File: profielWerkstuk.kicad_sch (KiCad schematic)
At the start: 0 parts

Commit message: added preselectors and antenna protection
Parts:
- added AE1: HF_ANT, symbol Device:Antenna
- added AE2: VHF_ANT, symbol Device:Antenna
- added C1, C3: 1.6n, symbol Device:C
- added C10, C12, C15: 200p, symbol Device:C
- added C11: 91p, symbol Device:C
- added C13, C17: 110p, symbol Device:C
- added C14, C16: 36p, symbol Device:C
- added C18, C22: 82p, symbol Device:C
- added C19, C21: 15p, symbol Device:C
- added C2: 680p, symbol Device:C
- added C20: 130p, symbol Device:C
- added C23, C27: 62p, symbol Device:C
- added C24, C26: 7.5p, symbol Device:C
- added C25: 100p, symbol Device:C
- added C4, C6: 820p, symbol Device:C
- added C5: 360p, symbol Device:C
- added C7, C9: 430p, symbol Device:C
- added C8: 180p, symbol Device:C
- added D1, D2: D, symbol Device:D
- added L1, L3: 2u, symbol Device:L
- added L10, L12, L19, L21: 240n, symbol Device:L
- added L11: 560, symbol Device:L
- added L13, L17: 110n, symbol Device:L
- added L14, L16: 330n, symbol Device:L
- added L15: 62n, symbol Device:L
- added L18, L22: 47n, symbol Device:L
- added L2: 4.7u, symbol Device:L
- added L20: 27n, symbol Device:L
- added L23, L27: 22n, symbol Device:L
- added L24, L26: 180n, symbol Device:L
- added L25: 13n, symbol Device:L
- added L4, L6: 1u, symbol Device:L
- added L5: 2.2u, symbol Device:L
- added L7, L9: 470n, symbol Device:L
- added L8: 1.1u, symbol Device:L
- added R1, R2: 1M, symbol Device:R
- added R3, R4, R5, R6, R7, R8, R9: 50, symbol Device:R
- added SW1: SW_HF/VHFa, symbol Switch:SW_SPDT
- added SW2: SW_ANT, symbol Switch:SW_SPDT
- added SW3: SW_PRESELECT_HFa, symbol Switch:SW_Rotary_1x4_MP
- added SW4, SW6: SW_Rotary_1x3_MP, symbol Switch:SW_Rotary_1x3_MP
- added SW5: SW_PRESELECT_HFb, symbol Switch:SW_Rotary_1x4_MP
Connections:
- new net: C22.1, L21.2, L22.1, SW6.2
- new net: R7.1, SW4.1
- new net: C13.1, C14.1, L13.1, R7.2
- new net: C15.1, C16.1, L14.2, L15.1
- new net: AE1.1 (A), R1.1, SW2.3 (C)
- new net: R3.1, SW3.1
- new net: C1.1, C2.1, L1.1, R3.2
- new net: C26.2, L26.1
- new net: C27.1, L26.2, L27.1, SW6.3
- new net: C23.1, C24.1, L23.1, R9.2
- new net: C17.1, L16.2, L17.1, SW6.1
- new net: C25.1, C26.1, L24.2, L25.1
- new net: C9.1, L8.2, L9.1, SW5.3
- new net: C19.2, L19.1
- new net: C20.1, C21.1, L19.2, L20.1
- new net: R5.1, SW3.3
- new net: C7.1, C8.1, L7.1, R5.2
- new net: AE2.1 (A), R2.1, SW2.1 (A)
- new net: C6.1, L5.2, L6.1, SW5.2
- new net: C16.2, L16.1
- new net: C10.1, C11.1, L10.1, R6.2
- new net: C11.2, L11.1
- new net: C18.1, C19.1, L18.1, R8.2
- new net: C2.2, L2.1
- new net: C14.2, L14.1
- new net: D1.2 (A), D2.1 (K), SW1.2 (B), SW2.2 (B)
- new net: C3.1, L2.2, L3.1, SW5.1
- new net: C12.1, L11.2, L12.1, SW5.4
- new net: R4.1, SW3.2
- new net: R6.1, SW3.4
- new net: SW1.1 (A), SW3.5
- new net: C21.2, L21.1
- new net: C4.1, C5.1, L4.1, R4.2
- new net: C8.2, L8.1
- new net: C24.2, L24.1
- new net: R8.1, SW4.2
- new net: R9.1, SW4.3
- new net: SW1.3 (C), SW4.4
- new net: C5.2, L5.1
- new net GNDPWR: D1.1 (K), D2.2 (A), R1.2, R2.2
- new net GNDREF: C1.2, C10.2, C12.2, C13.2, C15.2, C17.2, C18.2, C20.2, C22.2, C23.2, C25.2, C27.2, C3.2, C4.2, C6.2, C7.2, C9.2, L1.2, L10.2, L12.2, L13.2, L15.2, L17.2, L18.2, L20.2, L22.2, L23.2, L25.2, L27.2, L3.2, L4.2, L6.2, L7.2, L9.2, SW3.MP, SW4.MP, SW5.MP, SW6.MP
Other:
- note added: "HF"
- note added: "VHF"

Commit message: renamed VHF preselector switch
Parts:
- L11: value 560 -> 560n
- SW1: value SW_HF/VHFa -> SW_HF/VHF
- SW4: value SW_Rotary_1x3_MP -> SW_PRESELECT_VHFa
- SW6: value SW_Rotary_1x3_MP -> SW_PRESELECT_VHFb
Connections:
- net at AE1.1 (A), R1.1: now also SW2.1 (A); no longer SW2.3 (C)
- net at AE2.1 (A), R2.1: now also SW2.3 (C); no longer SW2.1 (A)
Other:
- moved on the sheet: SW2
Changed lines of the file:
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@@
 	(wire
 		(pts
+			(xy 238.76 25.4) (xy 256.54 25.4)
+		)
+		(stroke
+			(width 0)
+			(type default)
+		)
+	)
+	(wire
+		(pts
 			(xy 144.78 88.9) (xy 158.75 88.9)
 		)
@@
 	(wire
 		(pts
+			(xy 173.99 91.44) (xy 199.39 91.44)
+		)
+		(stroke
+			(width 0)
+			(type default)
+		)
+	)
+	(wire
+		(pts
 			(xy 134.62 121.92) (xy 133.35 121.92)
 		)
@@
 			)
 		)
-		(property "Value" "SW_Rotary_1x3_MP"
+		(property "Value" "SW_PRESELECT_VHFa"
 			(at 38.1 83.82 0)
 			(show_name no)
@@
 			)
 		)
-		(property "Value" "560"
+		(property "Value" "560n"
 			(at 185.42 67.31 90)
 			(show_name no)
@@
 			)
 		)
-		(property "Value" "SW_HF/VHFa"
+		(property "Value" "SW_HF/VHF"
 			(at 87.63 21.59 0)
 			(show_name no)
@@
 			)
 		)
-		(property "Value" "SW_Rotary_1x3_MP"
+		(property "Value" "SW_PRESELECT_VHFb"
 			(at 166.37 83.82 0)
 			(show_name no)
@@
 	(symbol
 		(lib_id "Switch:SW_SPDT")
-		(at 46.99 27.94 180)
+		(at 46.99 27.94 0)
+		(mirror y)
 		(unit 1)
 		(body_style 1)
@@
 		(in_pos_files yes)
 		(dnp no)
-		(fields_autoplaced yes)
 		(property "Reference" "SW2"
 			(at 46.99 19.05 0)
@@
 		)
 		(property "Datasheet" ""
-			(at 46.99 20.32 0)
+			(at 46.99 35.56 0)
 			(hide yes)
 			(show_name no)

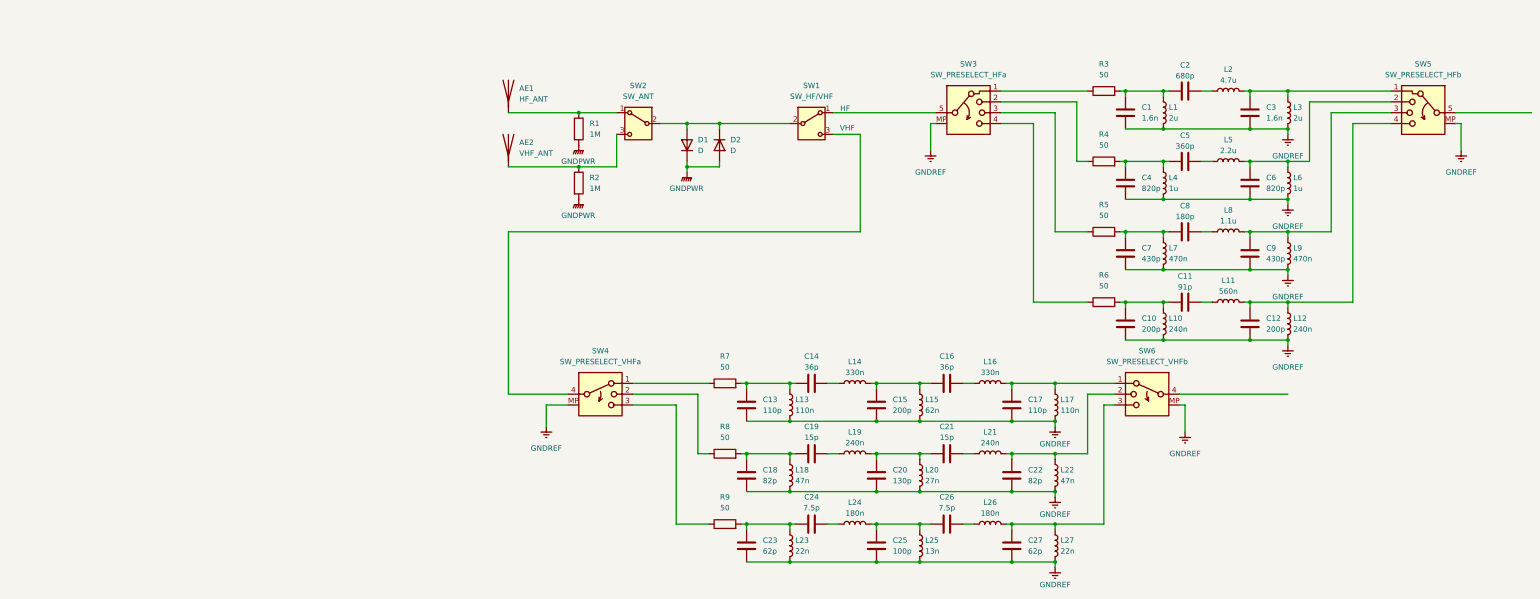
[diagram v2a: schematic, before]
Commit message: adjusted preselector values for overlap
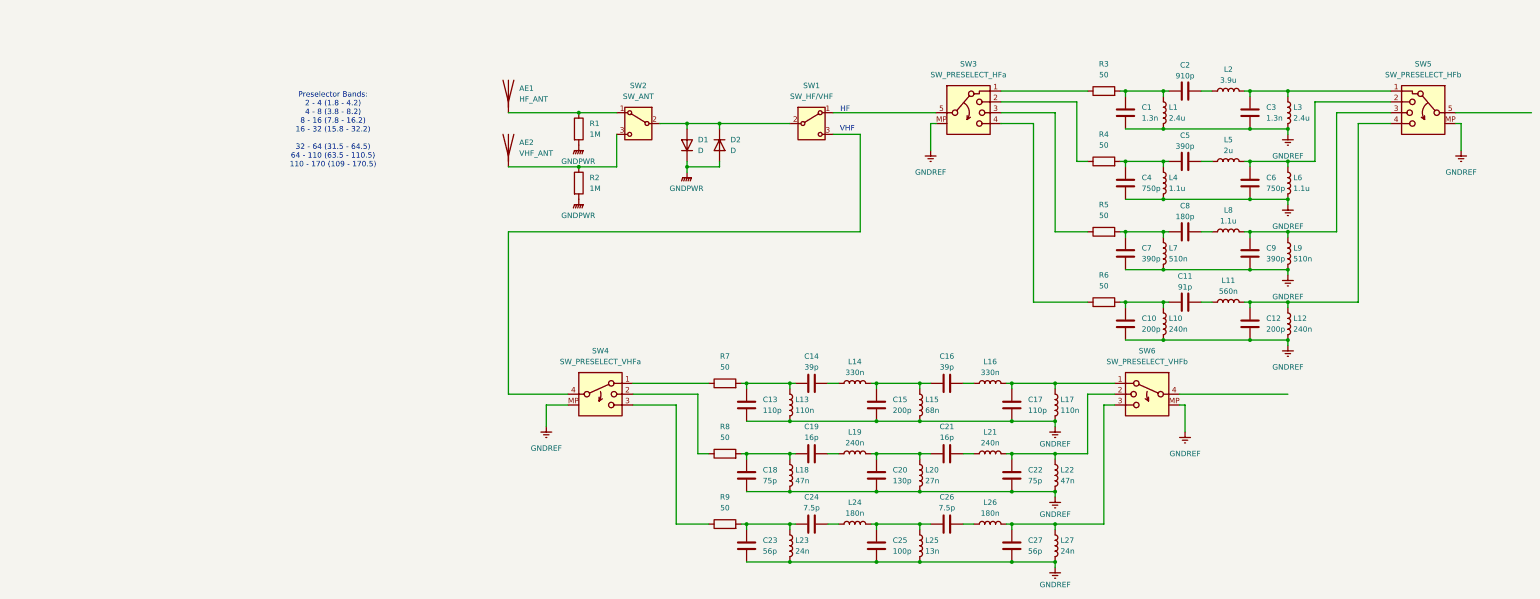
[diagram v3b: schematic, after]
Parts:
- C1, C3: value 1.6n -> 1.3n
- C14, C16: value 36p -> 39p
- C18, C22: value 82p -> 75p
- C19, C21: value 15p -> 16p
- C2: value 680p -> 910p
- C23, C27: value 62p -> 56p
- C4, C6: value 820p -> 750p
- C5: value 360p -> 390p
- C7, C9: value 430p -> 390p
- L1, L3: value 2u -> 2.4u
- L15: value 62n -> 68n
- L2: value 4.7u -> 3.9u
- L23, L27: value 22n -> 24n
- L4, L6: value 1u -> 1.1u
- L5: value 2.2u -> 2u
- L7, L9: value 470n -> 510n
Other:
- note added: "Preselector Bands: 2 - 4 (1.8 - 4.2) 4 - 8 (3.8 - 8.2) 8 - 16 (7.8 - 16.2) 16 - 32 (15.8 - 32.2) 32 - 64 (31.5 - 64.5) 64 - 110 (63.5 - 110.5) 110 - 170 (109 - 170.5)"
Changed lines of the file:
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@@
 	(generator_version "10.0")
 	(paper "A3")
+	(text "Preselector Bands:\n2 - 4 (1.8 - 4.2)\n4 - 8 (3.8 - 8.2)\n8 - 16 (7.8 - 16.2)\n16 - 32 (15.8 - 32.2)\n\n32 - 64 (31.5 - 64.5)\n64 - 110 (63.5 - 110.5)\n110 - 170 (109 - 170.5)"
+		(exclude_from_sim no)
+		(at -24.638 29.464 0)
+		(effects
+			(font
+				(size 1.27 1.27)
+			)
+		)
+	)
 	(text "HF"
 		(exclude_from_sim no)
@@
 	)
 	(junction
-		(at 199.39 36.83)
-		(diameter 0)
-		(color 0 0 0 0)
-	)
-	(junction
 		(at 102.87 105.41)
 		(diameter 0)
@@
 	)
 	(junction
+		(at 199.39 53.34)
+		(diameter 0)
+		(color 0 0 0 0)
+	)
+	(junction
 		(at 190.5 78.74)
 		(diameter 0)
@@
 	)
 	(junction
+		(at 199.39 36.83)
+		(diameter 0)
+		(color 0 0 0 0)
+	)
+	(junction
 		(at 33.02 25.4)
 		(diameter 0)
@@
 	)
 	(junction
-		(at 199.39 69.85)
-		(diameter 0)
-		(color 0 0 0 0)
-	)
-	(junction
 		(at 113.03 114.3)
 		(diameter 0)
@@
 	)
 	(junction
-		(at 82.55 105.41)
+		(at 199.39 69.85)
 		(diameter 0)
 		(color 0 0 0 0)
 	)
 	(junction
-		(at 144.78 88.9)
+		(at 82.55 105.41)
 		(diameter 0)
 		(color 0 0 0 0)
 	)
 	(junction
-		(at 199.39 53.34)
+		(at 144.78 88.9)
 		(diameter 0)
 		(color 0 0 0 0)
@@
 	(wire
 		(pts
-			(xy 204.47 22.86) (xy 223.52 22.86)
+			(xy 205.74 22.86) (xy 223.52 22.86)
 		)
 		(stroke
@@
 	(wire
 		(pts
-			(xy 204.47 36.83) (xy 204.47 22.86)
+			(xy 205.74 36.83) (xy 205.74 22.86)
 		)
 		(stroke
@@
 	(wire
 		(pts
-			(xy 214.63 69.85) (xy 199.39 69.85)
+			(xy 215.9 69.85) (xy 199.39 69.85)
 		)
 		(stroke
@@
 	(wire
 		(pts
-			(xy 199.39 36.83) (xy 204.47 36.83)
+			(xy 199.39 36.83) (xy 205.74 36.83)
 		)
 		(stroke
@@
 	(wire
 		(pts
-			(xy 223.52 27.94) (xy 214.63 27.94)
+			(xy 223.52 27.94) (xy 215.9 27.94)
 		)
 		(stroke
@@
 	(wire
 		(pts
-			(xy 209.55 25.4) (xy 209.55 53.34)
+			(xy 210.82 25.4) (xy 210.82 53.34)
 		)
 		(stroke
@@
 	(wire
 		(pts
-			(xy 209.55 53.34) (xy 199.39 53.34)
+			(xy 210.82 53.34) (xy 199.39 53.34)
 		)
 		(stroke
@@
 	(wire
 		(pts
-			(xy 214.63 27.94) (xy 214.63 69.85)
+			(xy 215.9 27.94) (xy 215.9 69.85)
 		)
 		(stroke
@@
 	(wire
 		(pts
-			(xy 223.52 25.4) (xy 209.55 25.4)
+			(xy 223.52 25.4) (xy 210.82 25.4)
 		)
 		(stroke
@@
 			)
 		)
-		(property "Value" "62n"
+		(property "Value" "68n"
 			(at 114.3 95.2499 0)
 			(show_name no)
@@
 			)
 		)
-		(property "Value" "22n"
+		(property "Value" "24n"
 			(at 83.82 128.2699 0)
 			(show_name no)
@@
 			)
 		)
-		(property "Value" "430p"
+		(property "Value" "390p"
 			(at 194.31 59.6899 0)
 			(show_name no)
@@
 			)
 		)
-		(property "Value" "820p"
+		(property "Value" "750p"
 			(at 194.31 43.1799 0)
 			(show_name no)
@@
 			)
 		)
-		(property "Value" "470n"
+		(property "Value" "510n"
 			(at 171.45 59.6899 0)
 			(show_name no)
@@
 			)
 		)
-		(property "Value" "430p"
+		(property "Value" "390p"
 			(at 165.1 59.6899 0)
 			(show_name no)
@@
 			)
 		)
-		(property "Value" "680p"
+		(property "Value" "910p"
 			(at 175.26 16.764 90)
 			(show_name no)
@@
 			)
 		)
-		(property "Value" "62p"
+		(property "Value" "56p"
 			(at 138.43 128.2699 0)
 			(show_name no)
@@
 			)
 		)
-		(property "Value" "36p"
+		(property "Value" "39p"
 			(at 87.63 85.09 90)
 			(show_name no)
@@
 			)
 		)
-		(property "Value" "22n"
+		(property "Value" "24n"
 			(at 146.05 128.2699 0)
 			(show_name no)
@@
 			)
 		)
-		(property "Value" "15p"
+		(property "Value" "16p"
 			(at 119.38 101.6 90)
 			(show_name no)
@@
 			)
 		)
-		(property "Value" "820p"
+		(property "Value" "750p"
 			(at 165.1 43.1799 0)
 			(show_name no)
@@
 			)
 		)
-		(property "Value" "2u"
+		(property "Value" "2.4u"
 			(at 171.45 26.6699 0)
 			(show_name no)
@@
 			)
 		)
-		(property "Value" "1u"
+		(property "Value" "1.1u"
 			(at 200.66 43.1799 0)
 			(show_name no)
@@
 			)
 		)
-		(property "Value" "1.6n"
+		(property "Value" "1.3n"
 			(at 165.1 26.6699 0)
 			(show_name no)
@@
 			)
 		)
-		(property "Value" "62p"
+		(property "Value" "56p"
 			(at 76.2 128.2699 0)
 			(show_name no)
@@
 			)
 		)
-		(property "Value" "1.6n"
+		(property "Value" "1.3n"
 			(at 194.31 26.6699 0)
 			(show_name no)
@@
 			)
 		)
-		(property "Value" "36p"
+		(property "Value" "39p"
 			(at 119.38 85.09 90)
 			(show_name no)
@@
 			)
 		)
-		(property "Value" "2.2u"
+		(property "Value" "2u"
 			(at 185.42 34.29 90)
 			(show_name no)
@@
 			)
 		)
-		(property "Value" "15p"
+		(property "Value" "16p"
 			(at 87.63 101.6 90)
 			(show_name no)
@@
 			)
 		)
-		(property "Value" "470n"
+		(property "Value" "510n"
 			(at 200.66 59.6899 0)
 			(show_name no)
@@
 			)
 		)
-		(property "Value" "82p"
+		(property "Value" "75p"
 			(at 138.43 111.7599 0)
 			(show_name no)
@@
 			)
 		)
-		(property "Value" "1u"
+		(property "Value" "1.1u"
 			(at 171.45 43.1799 0)
 			(show_name no)
@@
 			)
 		)
-		(property "Value" "2u"
+		(property "Value" "2.4u"
 			(at 200.66 26.6699 0)
 			(show_name no)
@@
 			)
 		)
-		(property "Value" "82p"
+		(property "Value" "75p"
 			(at 76.2 111.7599 0)
 			(show_name no)
@@
 			)
 		)
-		(property "Value" "360p"
+		(property "Value" "390p"
 			(at 175.26 33.274 90)
 			(show_name no)
@@
 			)
 		)
-		(property "Value" "4.7u"
+		(property "Value" "3.9u"
 			(at 185.42 17.78 90)
 			(show_name no)

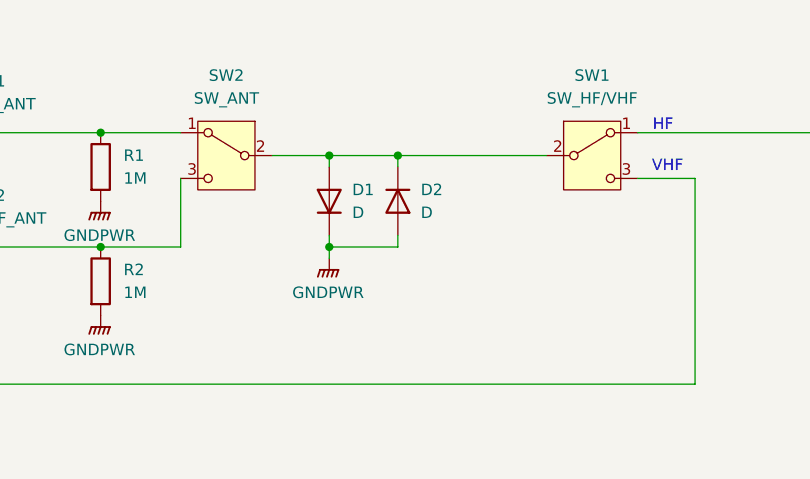
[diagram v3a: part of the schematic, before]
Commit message: switched protection diodes
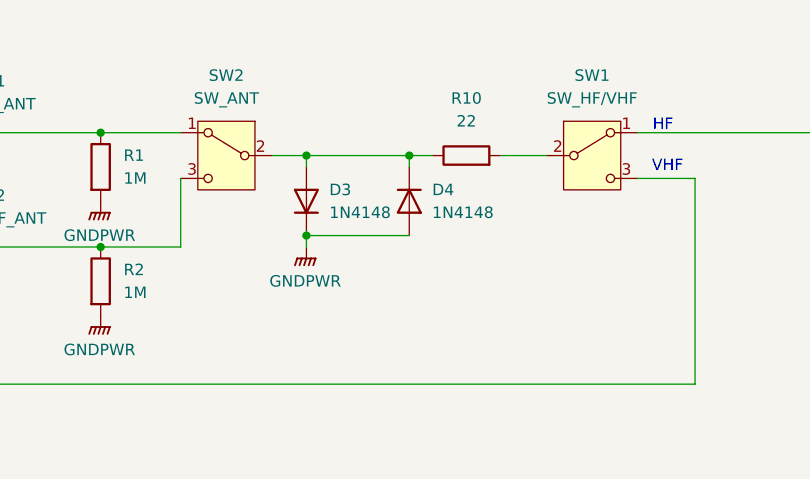
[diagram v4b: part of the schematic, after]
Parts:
- removed D1, D2: D, symbol Device:D
- added D3, D4: 1N4148, Diode_THT:D_DO-35_SOD27_P7.62mm_Horizontal, symbol Diode:1N4148
- added R10: 22, symbol Device:R
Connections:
- net GNDPWR: now also D3.1 (K), D4.2 (A)
- net at SW2.2 (B): now also D3.2 (A), D4.1 (K), R10.1; no longer SW1.2 (B)
- new net: R10.2, SW1.2 (B)

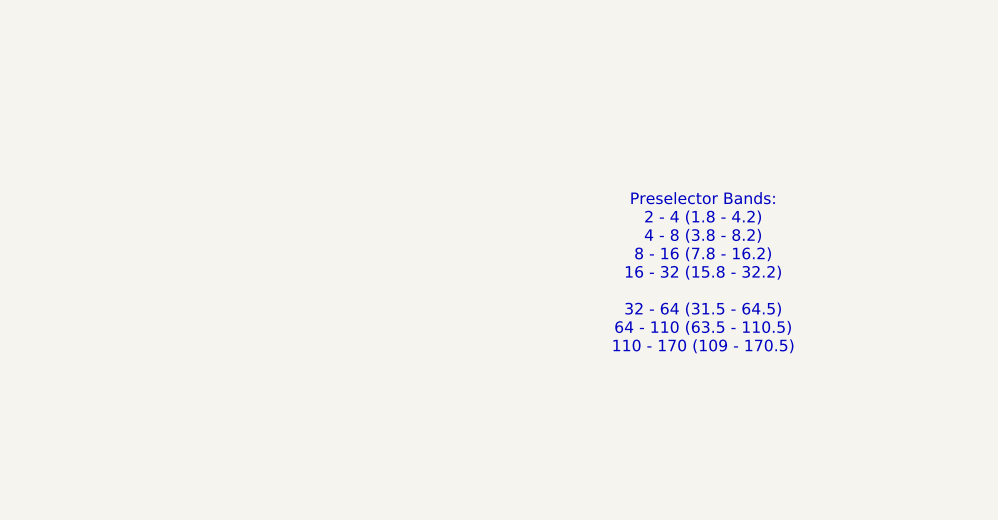
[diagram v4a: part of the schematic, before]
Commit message: added info text on the side
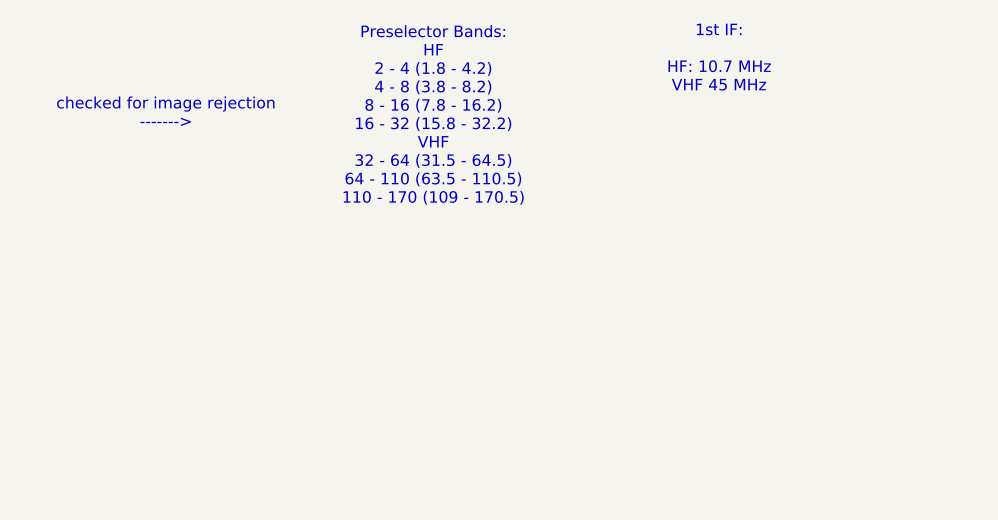
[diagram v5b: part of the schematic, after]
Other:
- note added: "1st IF: HF: 10.7 MHz VHF 45 MHz"
- note added: "Preselector Bands: HF 2 - 4 (1.8 - 4.2) 4 - 8 (3.8 - 8.2) 8 - 16 (7.8 - 16.2) 16 - 32 (15.8 - 32.2) VHF 32 - 64 (31.5 - 64.5) 64 - 110 (63.5 - 110.5) 110 - 170 (109 - 170.5)"
- note added: "checked for image rejection ------->"
- note removed: "Preselector Bands: 2 - 4 (1.8 - 4.2) 4 - 8 (3.8 - 8.2) 8 - 16 (7.8 - 16.2) 16 - 32 (15.8 - 32.2) 32 - 64 (31.5 - 64.5) 64 - 110 (63.5 - 110.5) 110 - 170 (109 - 170.5)"
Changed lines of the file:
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@@
 	(generator_version "10.0")
 	(paper "A3")
-	(text "Preselector Bands:\n2 - 4 (1.8 - 4.2)\n4 - 8 (3.8 - 8.2)\n8 - 16 (7.8 - 16.2)\n16 - 32 (15.8 - 32.2)\n\n32 - 64 (31.5 - 64.5)\n64 - 110 (63.5 - 110.5)\n110 - 170 (109 - 170.5)"
+	(text "Preselector Bands:\nHF\n2 - 4 (1.8 - 4.2)\n4 - 8 (3.8 - 8.2)\n8 - 16 (7.8 - 16.2)\n16 - 32 (15.8 - 32.2)\nVHF\n32 - 64 (31.5 - 64.5)\n64 - 110 (63.5 - 110.5)\n110 - 170 (109 - 170.5)"
 		(exclude_from_sim no)
-		(at -24.638 29.464 0)
+		(at -54.61 11.938 0)
 		(effects
 			(font
+				(size 1.27 1.27)
+			)
+		)
+	)
+	(text "checked for image rejection\n------->"
+		(exclude_from_sim no)
+		(at -84.328 11.684 0)
+		(effects
+			(font
+				(size 1.27 1.27)
+			)
+		)
+	)
+	(text "1st IF:\n\nHF: 10.7 MHz\nVHF 45 MHz\n"
+		(exclude_from_sim no)
+		(at -22.86 5.588 0)
+		(effects
+			(font

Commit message: started work on LNA
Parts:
- added Q1: 2N5179, symbol Transistor_BJT:Q_NPN_BCE
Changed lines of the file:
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@@
+	)
+	(symbol
+		(lib_id "Transistor_BJT:Q_NPN_BCE")
+		(at 199.39 123.19 0)
+		(unit 1)
+		(body_style 1)
+		(exclude_from_sim no)
+		(in_bom yes)
+		(on_board yes)
+		(in_pos_files yes)
+		(dnp no)
+		(fields_autoplaced yes)
+		(property "Reference" "Q1"
+			(at 204.47 121.9199 0)
+			(show_name no)
+			(do_not_autoplace no)
+			(effects
+				(font
+					(size 1.27 1.27)
+				)
+				(justify left)
+			)
+		)
+		(property "Value" "2N5179"
+			(at 204.47 124.4599 0)
+			(show_name no)
+			(do_not_autoplace no)
+			(effects
+				(font
+					(size 1.27 1.27)
+				)
+				(justify left)
+			)
+		)
+		(property "Footprint" ""
+			(at 204.47 120.65 0)
+			(hide yes)
+			(show_name no)
+			(do_not_autoplace no)
+			(effects
+				(font
+					(size 1.27 1.27)
+				)
+			)
+		)
+		(property "Datasheet" ""
+			(at 199.39 123.19 0)
+			(hide yes)
+			(show_name no)
+			(do_not_autoplace no)
+			(effects
+				(font
+					(size 1.27 1.27)
+				)
+			)
+		)
+		(property "Description" "NPN transistor, base/collector/emitter"
+			(at 199.39 123.19 0)
+			(hide yes)
+			(show_name no)
+			(do_not_autoplace no)
+			(effects
+				(font
+					(size 1.27 1.27)
+				)
+			)
+		)
+		(property "Sim.Device" "NPN"
+			(at 199.39 123.19 0)
+			(hide yes)
+			(show_name no)
+			(do_not_autoplace no)
+			(effects
+				(font
+					(size 1.27 1.27)
+				)
+			)
+		)
+		(property "Sim.Pins" "1=B 2=C 3=E"
+			(at 199.39 123.19 0)
+			(hide yes)
+			(show_name no)
+			(do_not_autoplace no)
+			(effects
+				(font
+					(size 1.27 1.27)
+				)
+			)
+		)
+		(pin "1"
+		)
+		(pin "3"
+		)
+		(pin "2"
+		)
+		(instances
+			(project "profielWerkstuk"
+				(path "/2ff6a573-99b7-4d75-b82d-04e5d220b6e6"
+					(reference "Q1")
+					(unit 1)
+				)
+			)
+		)
 	)
 	(symbol
